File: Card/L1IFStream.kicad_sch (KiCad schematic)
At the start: 107 parts, among them J1 Conn_Coaxial, J2 USB_A, J3 RF_Shield_One_Piece, J4 Conn_Coaxial, U1 MAX2769ETI+T, U10 74LVC374, U11 74HC2GU04, U2 TPS717285DCKR, U3 TPS717285DCKR, U4 NCP164CSN330T1G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

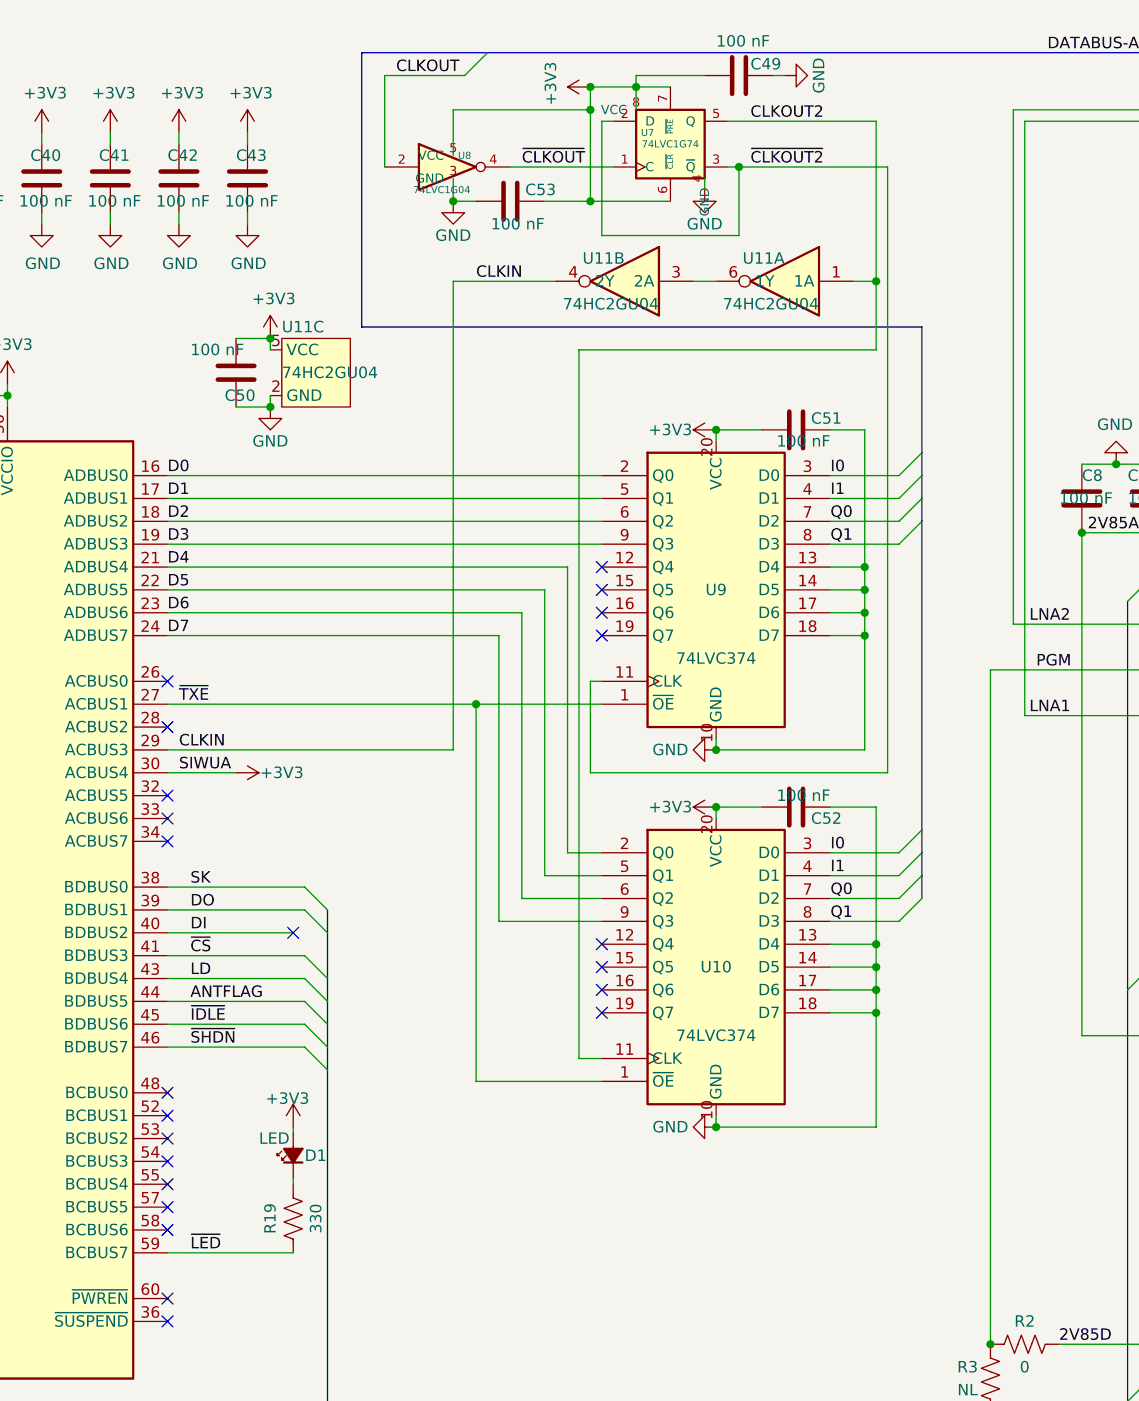
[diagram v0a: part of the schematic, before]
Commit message: Squared up L1IFTHMB and L1IFStream to implement the same nibble selector
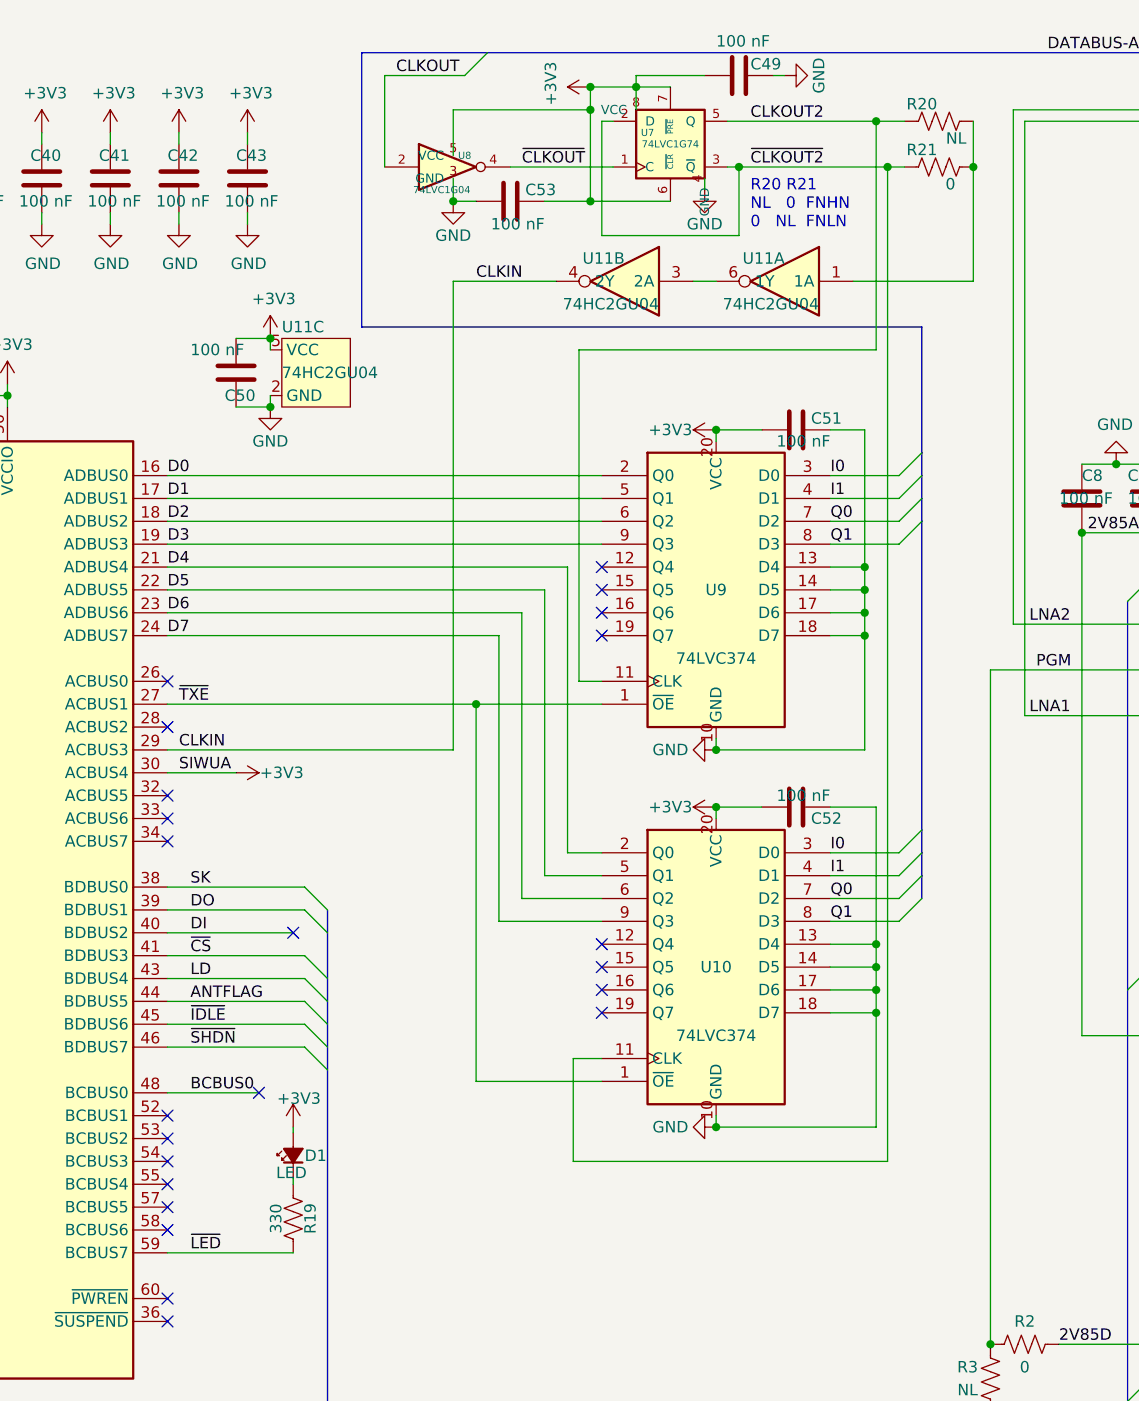
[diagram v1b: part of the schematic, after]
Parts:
- added R20: NL, L1IFStream:R_0603_1608Metric, symbol L1IFStream-rescue:R_US-MAX2769FT2232H
- added R21: 0, L1IFStream:R_0603_1608Metric, symbol L1IFStream-rescue:R_US-MAX2769FT2232H
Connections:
- net CLKOUT2: now also U9.11 (CLK), R20.2; no longer U10.11 (CLK), U11.1 (1A)
- net ~{CLKOUT2}: now also U10.11 (CLK), R21.2; no longer U9.11 (CLK)
- net BCBUS0: now reaches U6.48 (BCBUS0)
- new net: R20.1, R21.1, U11.1 (1A)
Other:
- note added: "R20 R21 NL 0 FNHN 0 NL FNLN"
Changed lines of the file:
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@@
   (title_block
     (title "L1 IF Stream")
-    (date "2023-10-24")
+    (date "2023-11-01")
     (rev "${SCH_VER}")
     (comment 1 "creativecommons.org/licenses/by/4.0/")
@@
     (comment 4 "Author: W. Kyle Gilbertson")
   )
+  (junction (at 224.79 27.94) (diameter 0) (color 0 0 0 0)
+  )
   (junction (at 331.47 78.74) (diameter 0) (color 0 0 0 0)
   )
@@
   (junction (at 205.74 57.15) (diameter 0) (color 0 0 0 0)
   )
-  (junction (at 223.52 40.64) (diameter 0) (color 0 0 0 0)
-  )
   (junction (at 33.02 62.23) (diameter 0) (color 0 0 0 0)
   )
@@
   (junction (at 402.59 132.08) (diameter 0) (color 0 0 0 0)
   )
+  (junction (at 223.52 22.86) (diameter 0) (color 0 0 0 0)
+  )
   (junction (at 82.55 67.31) (diameter 0) (color 0 0 0 0)
   )
@@
   (junction (at 156.21 54.61) (diameter 0) (color 0 0 0 0)
   )
+  (junction (at 234.315 27.94) (diameter 0) (color 0 0 0 0)
+  )
   (junction (at 271.78 116.84) (diameter 0) (color 0 0 0 0)
   )
@@
   (junction (at 417.83 19.05) (diameter 0) (color 0 0 0 0)
   )
-  (no_connect (at 144.78 130.81))
   (no_connect (at 144.78 85.09))
   (no_connect (at 193.04 119.38))
@@
   (no_connect (at 144.78 133.35))
   (no_connect (at 193.04 116.84))
+  (no_connect (at 154.94 130.81))
   (no_connect (at 193.04 114.3))
   (no_connect (at 257.81 63.5))
@@
     (stroke (width 0) (type default))
   )
+  (wire (pts (xy 144.78 130.81) (xy 154.94 130.81))
+    (stroke (width 0) (type default))
+  )
   (wire (pts (xy 402.59 132.08) (xy 405.13 132.08))
     (stroke (width 0) (type default))
@@
     (stroke (width 0) (type default))
   )
+  (wire (pts (xy 223.52 22.86) (xy 226.695 22.86))
+    (stroke (width 0) (type default))
+  )
   (wire (pts (xy 405.13 147.32) (xy 405.13 132.08))
     (stroke (width 0) (type default))
@@
     (stroke (width 0) (type default))
   )
+  (wire (pts (xy 234.315 22.86) (xy 234.315 27.94))
+    (stroke (width 0) (type default))
+  )
   (wire (pts (xy 81.28 35.56) (xy 95.25 35.56))
     (stroke (width 0) (type default))
@@
     (stroke (width 0) (type default))
   )
-  (wire (pts (xy 223.52 22.86) (xy 223.52 40.64))
-    (stroke (width 0) (type default))
-  )
   (wire (pts (xy 364.49 147.32) (xy 365.76 147.32))
     (stroke (width 0) (type default))
@@
     (stroke (width 0) (type default))
   )
-  (wire (pts (xy 190.5 127) (xy 193.04 127))
-    (stroke (width 0) (type default))
-  )
   (wire (pts (xy 218.44 64.77) (xy 226.06 64.77))
     (stroke (width 0) (type default))
@@
     (stroke (width 0) (type default))
   )
+  (wire (pts (xy 190.5 85.09) (xy 193.04 85.09))
+    (stroke (width 0) (type default))
+  )
   (wire (pts (xy 179.07 87.63) (xy 179.07 129.54))
     (stroke (width 0) (type default))
@@
     (stroke (width 0) (type default))
   )
-  (wire (pts (xy 191.77 85.09) (xy 191.77 95.25))
+  (wire (pts (xy 224.79 138.43) (xy 189.865 138.43))
     (stroke (width 0) (type default))
   )
@@
     (stroke (width 0) (type default))
   )
+  (wire (pts (xy 234.315 27.94) (xy 234.315 40.64))
+    (stroke (width 0) (type default))
+  )
   (wire (pts (xy 281.94 116.84) (xy 281.94 121.92))
     (stroke (width 0) (type default))
@@
     (stroke (width 0) (type default))
   )
+  (wire (pts (xy 223.52 22.86) (xy 223.52 48.26))
+    (stroke (width 0) (type default))
+  )
   (wire (pts (xy 124.46 53.34) (xy 127 53.34))
     (stroke (width 0) (type default))
@@
     (stroke (width 0) (type default))
   )
-  (wire (pts (xy 190.5 48.26) (xy 190.5 127))
+  (wire (pts (xy 190.5 48.26) (xy 190.5 85.09))
     (stroke (width 0) (type default))
   )
@@
     (stroke (width 0) (type default))
   )
+  (wire (pts (xy 189.865 127) (xy 193.04 127))
+    (stroke (width 0) (type default))
+  )
   (wire (pts (xy 417.83 66.04) (xy 417.83 158.75))
     (stroke (width 0) (type default))
@@
     (stroke (width 0) (type default))
   )
+  (wire (pts (xy 224.79 27.94) (xy 226.695 27.94))
+    (stroke (width 0) (type default))
+  )
   (wire (pts (xy 228.6 177.8) (xy 228.6 182.88))
     (stroke (width 0) (type default))
@@
     (stroke (width 0) (type default))
   )
-  (wire (pts (xy 193.04 85.09) (xy 191.77 85.09))
-    (stroke (width 0) (type default))
-  )
   (wire (pts (xy 184.15 109.22) (xy 184.15 77.47))
     (stroke (width 0) (type default))
@@
     (stroke (width 0) (type default))
   )
-  (wire (pts (xy 224.79 95.25) (xy 191.77 95.25))
-    (stroke (width 0) (type default))
-  )
   (wire (pts (xy 250.19 60.96) (xy 254 60.96))
     (stroke (width 0) (type default))
@@
     (stroke (width 0) (type default))
   )
-  (wire (pts (xy 220.98 40.64) (xy 223.52 40.64))
-    (stroke (width 0) (type default))
-  )
   (wire (pts (xy 275.59 167.64) (xy 275.59 173.99))
     (stroke (width 0) (type default))
@@
     (stroke (width 0) (type default))
   )
-  (wire (pts (xy 223.52 40.64) (xy 223.52 48.26))
-    (stroke (width 0) (type default))
-  )
   (wire (pts (xy 281.94 132.08) (xy 284.48 132.08))
     (stroke (width 0) (type default))
@@
     (stroke (width 0) (type default))
   )
+  (wire (pts (xy 189.865 127) (xy 189.865 138.43))
+    (stroke (width 0) (type default))
+  )
   (wire (pts (xy 121.92 54.61) (xy 121.92 53.34))
     (stroke (width 0) (type default))
@@
     (stroke (width 0) (type default))
   )
-  (wire (pts (xy 224.79 27.94) (xy 224.79 95.25))
-    (stroke (width 0) (type default))
-  )
   (wire (pts (xy 144.78 123.19) (xy 160.02 123.19))
     (stroke (width 0) (type default))
@@
     (stroke (width 0) (type default))
   )
+  (wire (pts (xy 220.98 40.64) (xy 234.315 40.64))
+    (stroke (width 0) (type default))
+  )
   (wire (pts (xy 323.85 222.25) (xy 323.85 220.98))
     (stroke (width 0) (type default))
@@
     (stroke (width 0) (type default))
   )
+  (wire (pts (xy 224.79 27.94) (xy 224.79 138.43))
+    (stroke (width 0) (type default))
+  )
   (wire (pts (xy 287.02 30.48) (xy 289.56 30.48))
     (stroke (width 0) (type default))
@@
     (effects (font (size 1.27 1.27)) (justify left bottom))
   )
+  (text "R20 R21\nNL   0  FNHN\n0   NL  FNLN\n" (at 209.55 34.925 0)
+    (effects (font (size 1.27 1.27)) (justify left bottom))
+  )
   (label "CLKIN" (at 146.05 92.71 0) (fields_autoplaced)
     (effects (font (size 1.27 1.27)) (justify left bottom))
@@
     (effects (font (size 1.27 1.27)) (justify left bottom))
   )
+  (label "BCBUS0" (at 147.32 130.81 0) (fields_autoplaced)
+    (effects (font (size 1.27 1.27)) (justify left bottom))
+  )
   (label "~{CLKOUT}" (at 184.15 27.94 0) (fields_autoplaced)
     (effects (font (size 1.27 1.27)) (justify left bottom))
@@
     )
   )
+  (symbol (lib_id "L1IFStream-rescue:R_US-MAX2769FT2232H") (at 230.505 27.94 270) (unit 1)
+    (in_bom yes) (on_board yes) (dnp no)
+    (property "Reference" "R21" (at 228.6 26.035 90)
+      (effects (font (size 1.27 1.27)))
+    )
+    (property "Value" "0" (at 231.775 29.845 90)
+      (effects (font (size 1.27 1.27)))
+    )
+    (property "Footprint" "L1IFStream:R_0603_1608Metric" (at 230.251 28.956 90)
+      (effects (font (size 1.27 1.27)) hide)
+    )
+    (property "Datasheet" "~" (at 230.505 27.94 0)
+      (effects (font (size 1.27 1.27)) hide)
+    )
+    (property "Description" "RES 0 OHM JUMPER 0603" (at 230.505 27.94 90)
+      (effects (font (size 1.27 1.27)) hide)
+    )
+    (property "Digi-Key" "2019-RK73Z1JTTDCT-ND" (at 230.505 27.94 90)
+      (effects (font (size 1.27 1.27)) hide)
+    )
+    (pin "1")
+    (pin "2")
+    (instances
+      (project "L1IFStream"
+        (path "/e22d8814-0b83-456b-8939-db783783fcf1"
+          (reference "R21") (unit 1)
+        )
+      )
+    )
+  )
   (symbol (lib_id "L1IFStream-rescue:74LVC374-MAX2769FT2232H") (at 205.74 116.84 0) (unit 1)
     (in_bom yes) (on_board yes) (dnp no)
@@
   (symbol (lib_id "L1IFStream-rescue:R_US-MAX2769FT2232H") (at 158.75 144.78 0) (unit 1)
     (in_bom yes) (on_board yes) (dnp no)
-    (property "Reference" "R19" (at 156.21 144.78 90)
+    (property "Reference" "R19" (at 160.655 144.78 90)
       (effects (font (size 1.27 1.27)))
     )
-    (property "Value" "330" (at 161.29 144.78 90)
+    (property "Value" "330" (at 156.845 144.78 90)
       (effects (font (size 1.27 1.27)))
     )
@@
       (effects (font (size 1.27 1.27)) hide)
     )
-    (property "Value" "+3V3" (at 158.115 131.445 0)
+    (property "Value" "+3V3" (at 159.385 131.445 0)
       (effects (font (size 1.27 1.27)))
     )
@@
     )
   )
+  (symbol (lib_id "L1IFStream-rescue:R_US-MAX2769FT2232H") (at 230.505 22.86 270) (unit 1)
+    (in_bom yes) (on_board yes) (dnp no)
+    (property "Reference" "R20" (at 228.6 20.955 90)
+      (effects (font (size 1.27 1.27)))
+    )
+    (property "Value" "NL" (at 232.41 24.765 90)
+      (effects (font (size 1.27 1.27)))
+    )
+    (property "Footprint" "L1IFStream:R_0603_1608Metric" (at 230.251 23.876 90)
+      (effects (font (size 1.27 1.27)) hide)
+    )
+    (property "Datasheet" "~" (at 230.505 22.86 0)
+      (effects (font (size 1.27 1.27)) hide)
+    )
+    (property "Description" "RES 0 OHM JUMPER 0603" (at 230.505 22.86 90)
+      (effects (font (size 1.27 1.27)) hide)
+    )
+    (property "Digi-Key" "2019-RK73Z1JTTDCT-ND" (at 230.505 22.86 90)
+      (effects (font (size 1.27 1.27)) hide)
+    )
+    (pin "1")
+    (pin "2")
+    (instances
+      (project "L1IFStream"
+        (path "/e22d8814-0b83-456b-8939-db783783fcf1"
+          (reference "R20") (unit 1)
+        )
+      )
+    )
+  )
   (symbol (lib_id "L1IFStream:SIT5156AICFA-30N0-16.368000_1") (at 328.93 40.64 0) (mirror y) (unit 1)
     (in_bom yes) (on_board yes) (dnp no)
@@
       (effects (font (size 1.27 1.27)) (justify right))
     )
-    (property "Value" "LED" (at 154.94 135.89 90)
+    (property "Value" "LED" (at 156.845 139.7 90)
       (effects (font (size 1.27 1.27)) (justify right))
     )
